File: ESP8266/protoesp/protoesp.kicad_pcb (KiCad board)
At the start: 2 copper layers, 97.5 x 90 mm, 192 parts, among them CN1 EPINS_TOP, CN10 USB_CURSED, CN11 CH_SPI, CN12 CH_I2C, CN13 CH341_PROG, CN14 CH_PROG, CN2 EPINS_BOTTOM, CN20 BATT, CN3 ESP_PROG, CN30 BUTTON_CONN, CN31 LDR_CONN, CN32 RGB_CONN, CN33 595_CONN, CN34 595_OUTS, CN35 595CHAIN_CONN, CN36 E_I2C, CN37 E_SPI, CN38 DRV_CONN, J1 0R, J11 0R, J17 0R, J19 0R, J2 0R, J22 0R, J7 0R, J8 0R, J9 0R, P1 PROTO_SPACE, Q1 BC817, Q2 CJ2305, SW1 RST, SW2 BUTTON, U1 CH341, U2 AP1117-33, U3 LTH7R, U4 74HC595, U5 AP2112K-3.3, U6 ESP32-WROOM-32, Y1 12MHz

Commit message: Final changes - only small silk art things left before I'll order it, otherwise, this is orderable!
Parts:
- added C17: 100nF, Capacitor_SMD:C_0805_2012Metric, B.Cu at (71.2, 71.8)
- added C18: 100nF, Capacitor_SMD:C_0805_2012Metric, B.Cu at (77.9, 71.3)
- added C19: 100nF, Capacitor_SMD:C_0805_2012Metric, F.Cu at (139.8, 51.1)
- added CN4: EPINS_TOP_E, Connector_PinHeader_2.54mm:PinHeader_1x04_P2.54mm_Vertical, F.Cu at (124.7, 55.6)
- added CN5: EPINS_BOTTOM_E, Connector_PinHeader_2.54mm:PinHeader_1x04_P2.54mm_Vertical, F.Cu at (124.7, 83.6)
- added FID1: Fiducial, Fiducial:Fiducial_1mm_Mask2mm, F.Cu at (71.1, 59.0)
- added FID2: Fiducial, Fiducial:Fiducial_1mm_Mask2mm, F.Cu at (129.7, 69.6)
- added FID3: Fiducial, Fiducial:Fiducial_1mm_Mask2mm, F.Cu at (116.2, 115.2)
- added FID4: Fiducial, Fiducial:Fiducial_1mm_Mask2mm, F.Cu at (57.5, 124.5)
- added G***: LOGO, protoesp:ey, F.Cu at (138.2, 69.4)
- added H1: MountingHole, MountingHole:MountingHole_3.2mm_M3, F.Cu at (60.9, 57.3)
- added H1: pin_hole, protoesp:PinHole_1,5mm, F.Cu at (52.5, 91.6)
- added H1: pin_hole, protoesp:PinHole_1,5mm, F.Cu at (52.5, 94.5)
- added H1: pin_hole, protoesp:PinHole_1,5mm, F.Cu at (98.0, 54.6)
- added H1: pin_hole, protoesp:PinHole_1,5mm, F.Cu at (95.4, 54.6)
- added H2: MountingHole, MountingHole:MountingHole_3.2mm_M3, F.Cu at (52.5, 137.5)
- added H3: MountingHole, MountingHole:MountingHole_3.2mm_M3, F.Cu at (145.5, 52.0)
- added H4: MountingHole, MountingHole:MountingHole_3.2mm_M3, F.Cu at (145.7, 124.9)
- added Q3: BC817, Package_TO_SOT_SMD:SOT-23, F.Cu at (77.8, 80.1)
- added Q4: BC817, Package_TO_SOT_SMD:SOT-23, F.Cu at (77.8, 76.8)
- added R22: 4K7, Resistor_SMD:R_0603_1608Metric, F.Cu at (122.2, 74.5)
- added R23: 1K8, Resistor_SMD:R_0603_1608Metric, F.Cu at (140.7, 132.6)
- added R24: 1K8, Resistor_SMD:R_0603_1608Metric, F.Cu at (140.6, 129.4)
- added R25: 4K7, Resistor_SMD:R_0603_1608Metric, F.Cu at (75.4, 80.0)
- added R26: 4K7, Resistor_SMD:R_0603_1608Metric, F.Cu at (75.4, 76.8)
- added SW3: GP0, Button_Switch_SMD:SW_SPST_SKQG_WithStem, F.Cu at (121.2, 79.0)
- SW1: value RST -> EN
- TP7: value B+ -> B-
- moved R18 8.76 mm to (67.1, 76.4), turned to 0 degrees
- moved REF** 2.70 mm to (50.5, 76.5), turned to 0 degrees
- moved REF** 2.70 mm to (50.5, 56.5), turned to 0 degrees
- moved D10 2.19 mm to (70.5, 76.5), turned to 0 degrees
- moved C2 1.61 mm to (56.6, 81.2)
- moved Y1 1.61 mm to (60.4, 77.4)
- moved C1 1.61 mm to (59.7, 81.2)
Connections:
- net CH_RST renamed CH_EN
- net Net-(CN38-Pad1) renamed DRV+
- net Net-(D11-Pad2) renamed DRV-
- CN1 pad 2: POT -> IO39
- CN1 pad 3: IO12 -> IO32
- CN12 pad 4: Net-(CN12-Pad4) -> CH_~RTS
- CN3 pad 6: BUTTON -> E_GP0
- NT6 pad 2: BUTTON -> E_GP0
- U6 pad 14: IO12 -> BUTTON
- U6 pad 25: BUTTON -> E_GP0
- U6 pad 4: POT -> LIGHT
- U6 pad 5: LIGHT -> IO39
- U6 pad 8: Net-(U6-Pad8) -> IO32
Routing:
- net CH_~RTS: track 7.35 -> 47.0 mm, vias 0 -> 4
- net E_GP0: track 0.00 -> 36.4 mm, vias 0 -> 1
- net GND: track 197.0 -> 227.6 mm, vias 118 -> 134
- net CH_MOSI: track 28.8 -> 56.9 mm, vias 1 -> 3
- net IO12: track 18.3 -> 0.00 mm, vias 1 -> 0
- net +3V3: track 336.4 -> 353.8 mm, vias 8 -> 10
- net E_SCL: track 76.5 -> 87.8 mm, vias 1 -> 2
- net 595_CLK: track 100.8 -> 110.9 mm
- net E_SDA: track 70.4 -> 79.1 mm, vias 1 -> 2
- net LED_RED: track 104.8 -> 113.1 mm, vias 3 -> 4
- net 595_LAT: track 85.8 -> 93.1 mm
- net IO32: track 0.00 -> 6.76 mm, vias 0 -> 1
- net CH_GP0: track 11.6 -> 18.2 mm
- net E_EN: track 78.9 -> 85.3 mm
- net CH_EN: track 12.3 -> 18.6 mm
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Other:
- board text added: "+"
- board text added: "-"
- board text added: "- ESP32-WROOM - Button - Light sensor - RGB LED - NPN driver - 595 shift register - I2C/SPI/GPIO expansion - Battery power - Proto space - USB-UART - WEMOS headers - Optional USB-I2C&SPI"
- board text added: "23 19 18 17"
- board text added: "3.3V"
- board text added: "CH-I2C"
- board text added: "CH-SPI"
- board text added: "CH340/1"
- board text added: "CMOSI CMISO CCLK CCS CVCC GND"
- board text added: "EN G39 G12 G23 G19 G18 G17 GND 3.3V G25 G26 G27"
- board text added: "ESP32"
- board text added: "GND 3.3V CS SCK SO SI"
- board text added: "GND ACT CVCC CSDA CSCL NC GND"
- board text added: "GND INT SCL SDA 3.3V"
- board text added: "GP12"
- board text added: "GP2"
- board text added: "GP21 22 16"
- board text added: "GP36"
- board text added: "I2C/GPIO header"
- board text added: "INT 3V3 GND GND VSW"
- board text added: "Part of the FANGY project."
- board text added: "ProtoESP ESP32 PCB v1"
- board text added: "ProtoESP protoSpace PCB v1"
- board text added: "RST"
- board text added: "SCL SDA"
- board text added: "SPI/GPIO header"
- board text added: "TXD RXD G5 G4 G16 G2 GND VSW G0 G15 G14 G13"
- board text added: "This PCB houses an ESP32 and a family of fun things for your learning, leisure and helpful purposes. I hope that this PCB becomes your friend. -A"
- board text added: "USB-UART"
- board text added: "VSW = 3.5V-5V"
- board text added: "VSW GND GND 3V3 INT"
- board text added: "Will you be a good or a bad proto?"
- board text added: "batt ery input"
- board text added: "rightmost 8-pin headers have Wemos-y pinout"
- board text added: "spaaaaace"
- board text removed: "GND ACT CVCC CSDA CSCL NC GND CMOSI CMISO CCLK CCS CVCC GND"
- board text removed: "GP0"
- board text removed: "GP35"
- board text removed: "bat tery in put"

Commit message: Latest updates - consider this v1.1 ;-P
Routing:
- net GND: track 227.6 -> 244.0 mm, vias 134 -> 140
- net +VSW: vias 9 -> 8
- net +5V: vias 5 -> 3

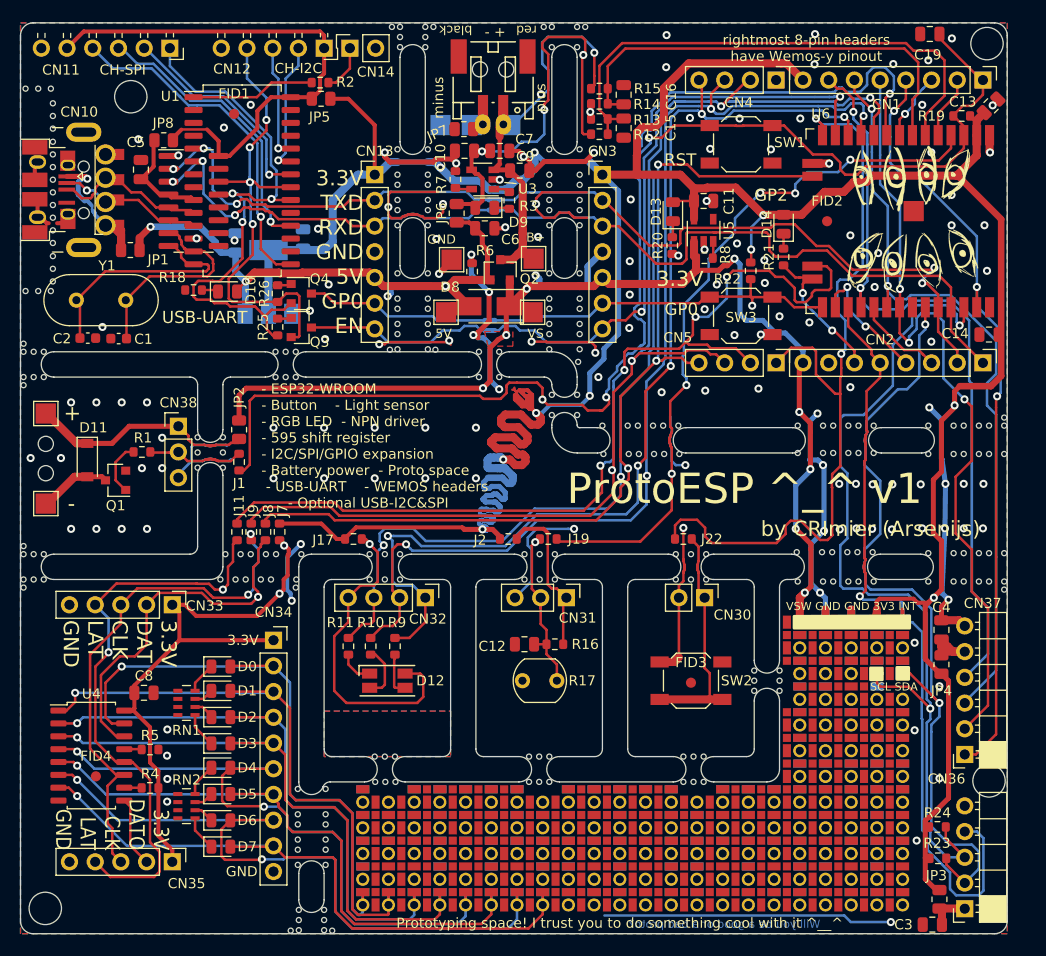
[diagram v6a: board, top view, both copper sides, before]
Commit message: [x] resistors inline with UART [x] add TX&RX LEDs [x] add longesp support [x] JLC tooling holes [x] PTH the driver PCB holes [x] space core on silkscreen
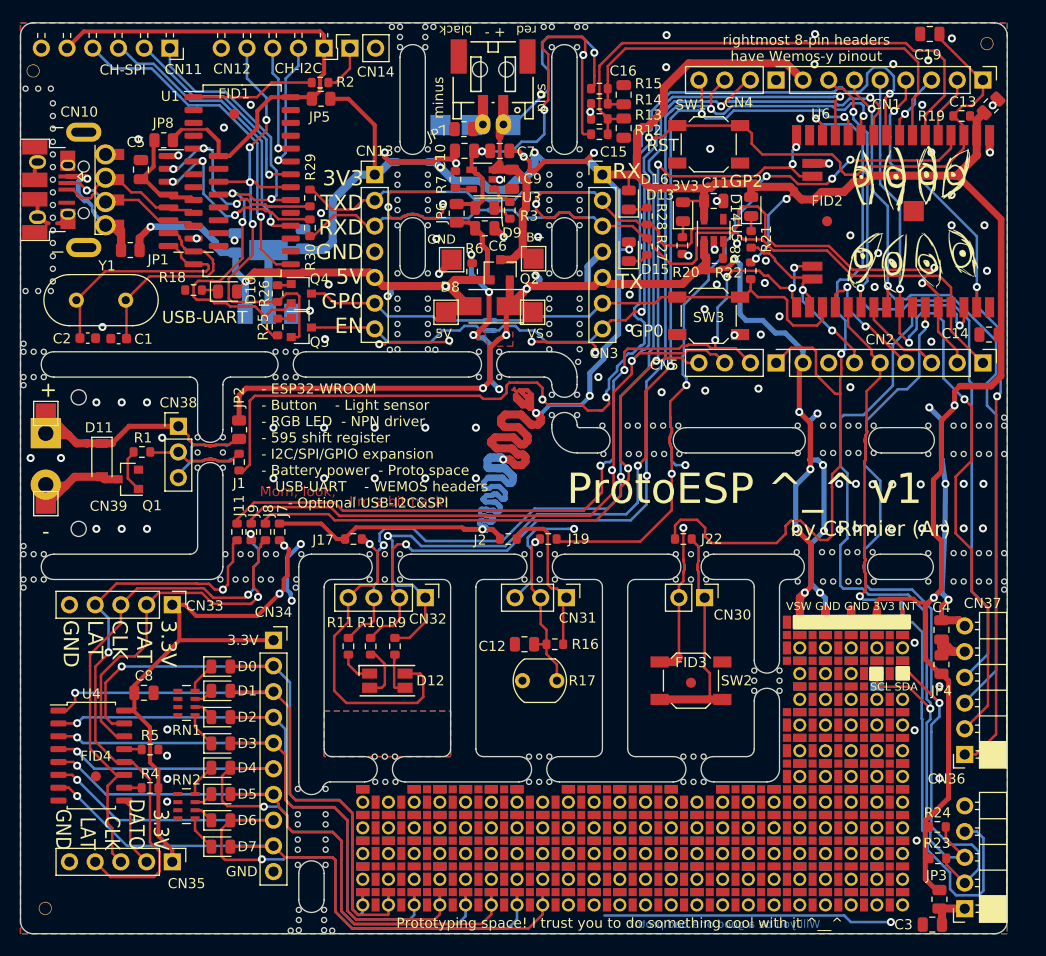
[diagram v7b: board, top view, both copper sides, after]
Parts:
- removed the H1 at (60.9, 57.3)
- removed the H1 at (52.5, 91.6)
- added CN39: DRV, TerminalBlock:TerminalBlock_bornier-2_P5.08mm, F.Cu at (52.5, 90.5)
- added D15: LED_TX, LED_SMD:LED_0805_2012Metric, F.Cu at (110.1, 72.6)
- added D16: LED_RX, LED_SMD:LED_0805_2012Metric, F.Cu at (110.1, 67.5)
- added G***: LOGO, protoesp:spaaaace, B.Cu at (126.1, 69.6)
- added H1: MountingHole, protoesp:JLCPCBToolingHole, F.Cu at (51.2, 54.8)
- added H1: pin_hole, protoesp:PinHole_1,5mm, F.Cu at (55.8, 87.0)
- added R27: 1K8, Resistor_SMD:R_0603_1608Metric, F.Cu at (111.9, 72.1)
- added R28: 1K8, Resistor_SMD:R_0603_1608Metric, F.Cu at (111.9, 69.1)
- added R29: 1K8, Resistor_SMD:R_0603_1608Metric, F.Cu at (78.6, 67.3)
- added R30: 1K8, Resistor_SMD:R_0603_1608Metric, F.Cu at (78.6, 70.2)
- H2, H3: value MountingHole -> ToolingHole; footprint MountingHole:MountingHole_3.2mm_M3 -> protoesp:JLCPCBToolingHole
- H4: footprint MountingHole:MountingHole_3.2mm_M3 -> protoesp:JLCPCBToolingHole
- moved H4 13.4 mm to (145.8, 138.2)
- moved H1 6.39 mm to (55.8, 100.0)
- moved D14 3.65 mm to (122.2, 68.2)
- moved R21 3.65 mm to (122.2, 71.4)
- moved SW1 3.20 mm to (118.0, 62.0)
- moved SW3 3.20 mm to (118.0, 79.0)
- moved D11 1.45 mm to (58.0, 93.2)
- moved Q1 1.25 mm to (60.6, 95.1)
- moved C9 1.15 mm to (98.5, 65.5), turned to 270 degrees
- moved C11 1.00 mm to (118.5, 67.6)
- moved D13 1.00 mm to (115.5, 68.7)
- moved R20 1.00 mm to (115.4, 72.0)
- moved R8 1.00 mm to (118.6, 73.2)
- moved U5 1.00 mm to (118.5, 70.5)
- moved R3 0.98 mm to (98.3, 68.5)
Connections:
- U1 pad 5: CH_TXD -> TXD
- U1 pad 6: CH_RXD -> RXD
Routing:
- net TXD: track 0.00 -> 21.3 mm, vias 0 -> 3
- net RXD: track 0.00 -> 21.2 mm, vias 0 -> 3
- net CH_TXD: track 40.0 -> 19.6 mm, vias 3 -> 0
- net CH_RXD: track 40.1 -> 19.9 mm, vias 3 -> 0
- net +3V3: track 353.9 -> 361.3 mm, vias 10 -> 11
- net DRV+: track 22.1 -> 29.2 mm
- net LED_ESP: track 14.6 -> 20.9 mm
- net DRV-: track 7.14 -> 12.7 mm
- net 595_LAT: track 93.1 -> 87.9 mm, vias 4 -> 6
- net E_RXD: track 60.6 -> 64.8 mm
- net 595_DAT: track 92.9 -> 97.1 mm, vias 3 -> 5
- net E_GP0: track 36.4 -> 38.9 mm, vias 1 -> 0
- net Net-(D15-Pad1): track 0.00 -> 2.05 mm
- net +VSW: track 111.7 -> 113.7 mm
- net Net-(D16-Pad1): track 0.00 -> 1.87 mm
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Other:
- board text added: "3V3"
- board text added: "3V3 TXD RXD GND 5V GP0 EN"
- board text added: "EN"
- board text added: "G39 G12 G23 G19 G18 G17 GND 3.3V G25 G26 G27"
- board text added: "I'm a bitmask!"
- board text added: "Mom, look,"
- board text added: "RX"
- board text added: "TX"
- board text added: "by CRImier (Ar)"
- board text removed: "EN G39 G12 G23 G19 G18 G17 GND 3.3V G25 G26 G27"
- board text removed: "by CRImier (Arsenijs)"

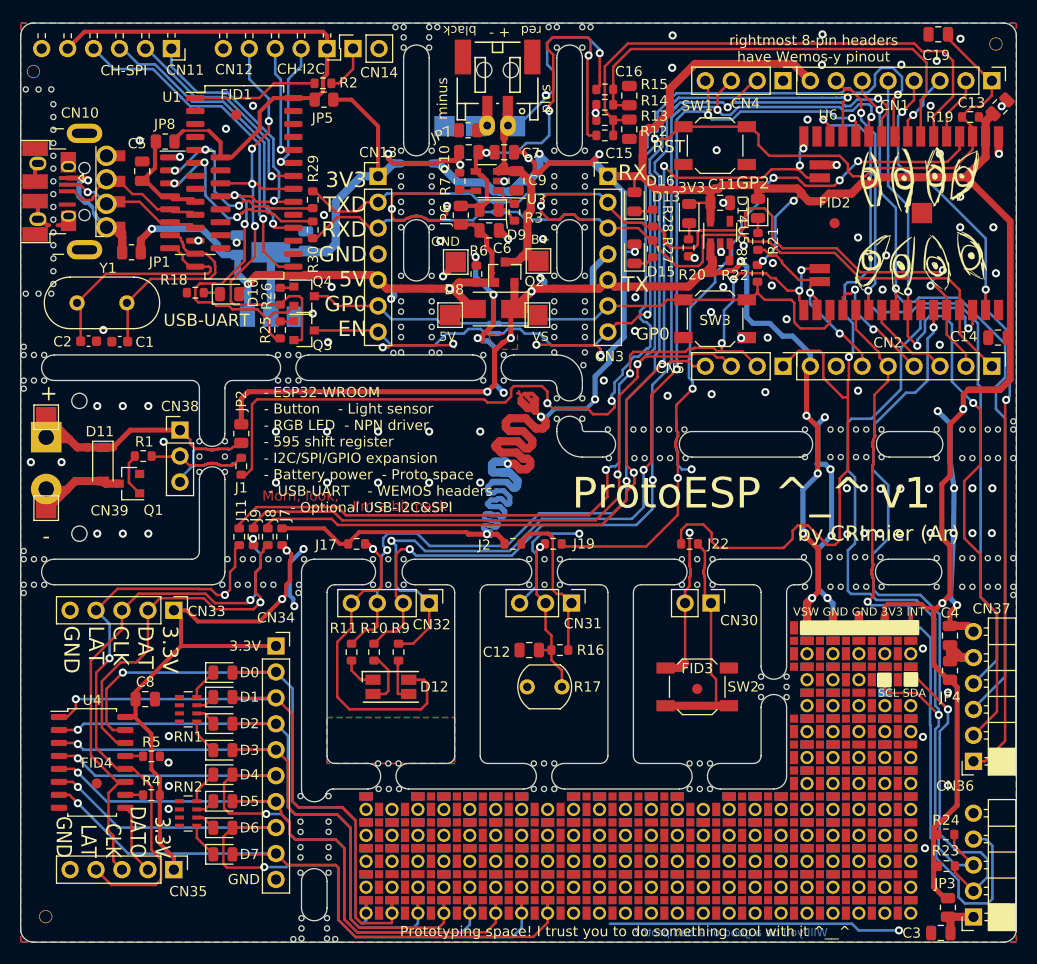
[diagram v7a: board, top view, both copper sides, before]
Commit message: protoesp: added battery onboard fuse, updated to KiCad6, small script tweaks, changed name
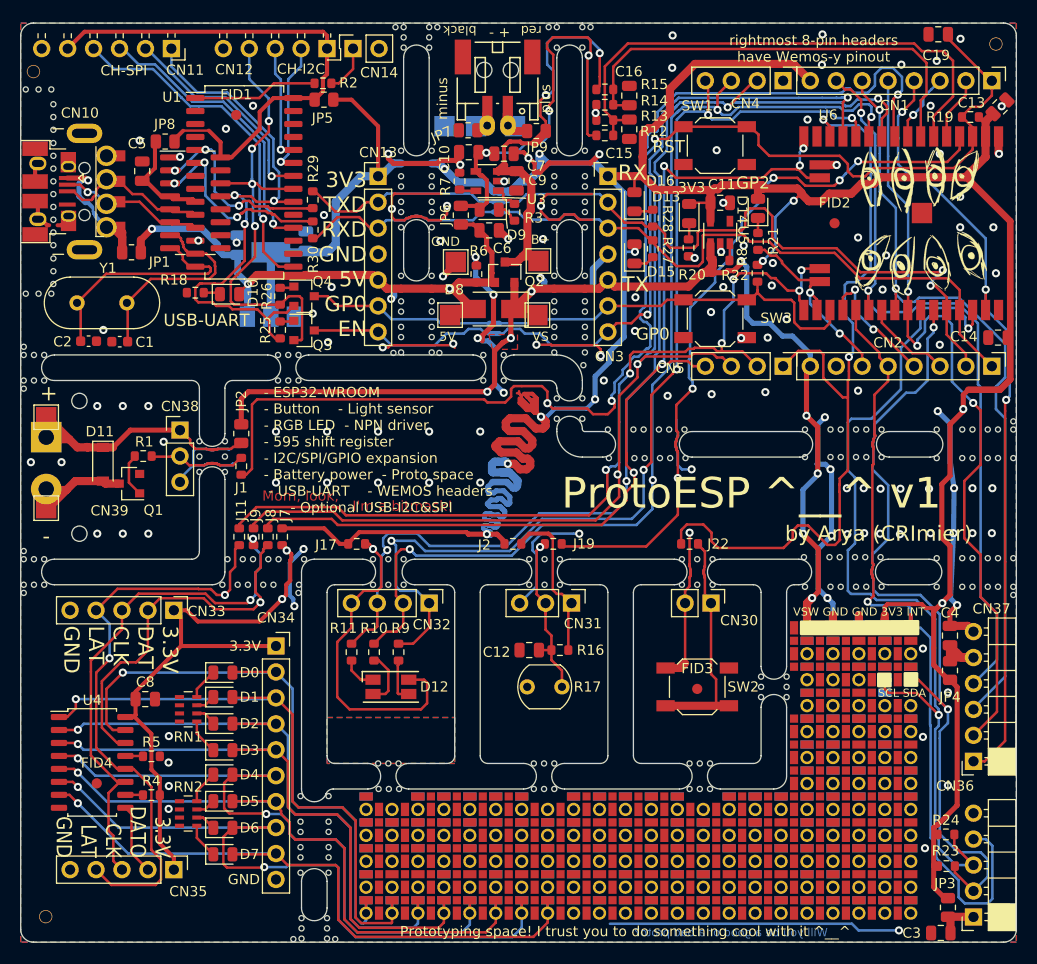
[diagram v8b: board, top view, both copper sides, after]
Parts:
- added JP9: 0R, Resistor_SMD:R_0805_2012Metric, F.Cu at (100.5, 60.6)
- moved C7 0.15 mm to (97.3, 62.8)
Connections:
- net CH_~RTS renamed CH_~{RTS}
- CN20 pad 1: +BATT -> BATT_IN+
- TP8 pad 1: +BATT -> BATT_IN+
- U1 pad 16: Net-(U1-Pad16) -> unconnected-(U1-Pad16)
- U1 pad 17: Net-(U1-Pad17) -> unconnected-(U1-Pad17)
- U1 pad 19: Net-(U1-Pad19) -> unconnected-(U1-Pad19)
- U1 pad 2: Net-(U1-Pad2) -> unconnected-(U1-Pad2)
- U1 pad 25: Net-(U1-Pad25) -> unconnected-(U1-Pad25)
- U1 pad 26: Net-(U1-Pad26) -> unconnected-(U1-Pad26)
- U1 pad 27: Net-(U1-Pad27) -> unconnected-(U1-Pad27)
- U1 pad 3: Net-(U1-Pad3) -> unconnected-(U1-Pad3)
- U1 pad 4: Net-(U1-Pad4) -> unconnected-(U1-Pad4)
- U1 pad 7: Net-(U1-Pad7) -> unconnected-(U1-Pad7)
- U1 pad 8: Net-(U1-Pad8) -> unconnected-(U1-Pad8)
- U5 pad 4: Net-(U5-Pad4) -> unconnected-(U5-Pad4)
- U6 pad 32: Net-(U6-Pad32) -> unconnected-(U6-Pad32)
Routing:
- net BATT_IN+: track 0.00 -> 5.46 mm
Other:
- net class Default removed
- board text added: "ProtoESP ^__^ v1"
- board text added: "by Arya (CRImier)"
- board text added: "~"
- board text removed: "ProtoESP ^_^ v1"
- board text removed: "by CRImier (Ar)"
- board text removed: "~~"
